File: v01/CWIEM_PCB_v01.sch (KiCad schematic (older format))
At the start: 10 parts

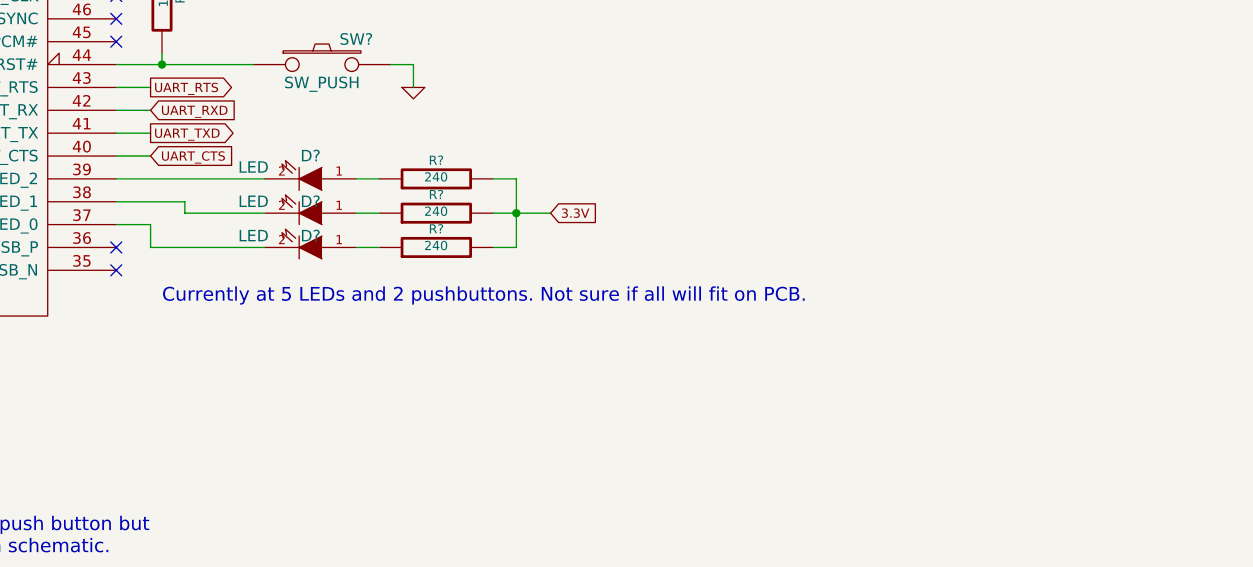
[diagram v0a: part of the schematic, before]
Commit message: Basically just added a single DIP switch to battery charging circuit.
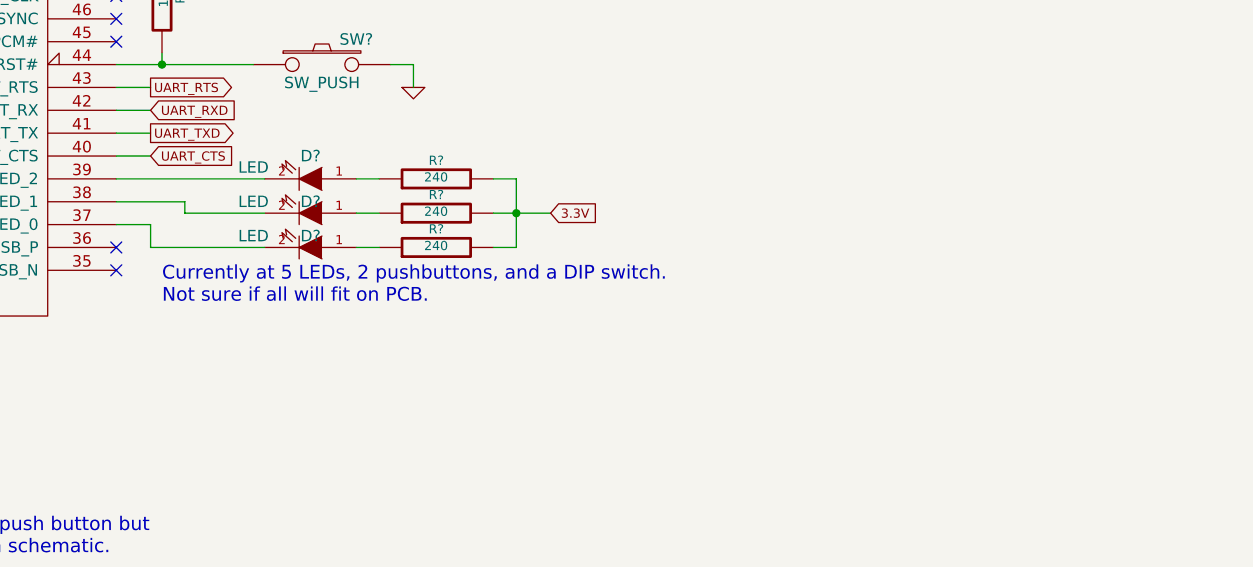
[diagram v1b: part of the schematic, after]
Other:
- note added: "Currently at 5 LEDs, 2 pushbuttons, and a DIP switch. \nNot sure if all will fit on PCB."
- note removed: "Currently at 5 LEDs and 2 pushbuttons. Not sure if all will fit on PCB."
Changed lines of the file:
@@
 Sheet 1 4
 Title "BC127 circuit"
-Date "12 oct 2014"
+Date "18 oct 2014"
 Rev "0"
 Comp ""
@@
 	8050 4300 7950 4300
 Text Notes 7100 4550 0    60   ~ 0
-Currently at 5 LEDs and 2 pushbuttons. Not sure if all will fit on PCB.
+Currently at 5 LEDs, 2 pushbuttons, and a DIP switch. \nNot sure if all will fit on PCB.
 Text Notes 5750 5650 0    60   ~ 0
 There is a mini push button but \nit looks weird in schematic.

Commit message: ERC.
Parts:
- gave numbers to parts that had none: 10
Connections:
- net UART_TXD: no longer U1.29 (CHG_EXT)
- net 3V3_USB: no longer names the net of U1.34 (3V3_USB)
- new net CHG_EXT: U1.29 (CHG_EXT)
- no-connect marks 24 -> 25
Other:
- note added: "I had to make CHG_EXT an output pin \n(base of PNP transistor is an input pin)."
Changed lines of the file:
@@
 Sheet 1 4
 Title "BC127 circuit"
-Date "18 oct 2014"
+Date "25 oct 2014"
 Rev "0"
 Comp ""
@@
 $EndDescr
 $Comp
-L BC127 U?
+L BC127 U1
 U 1 1 541DFC48
 P 5500 3400
-F 0 "U?" H 5500 3300 50  0000 C CNN
+F 0 "U1" H 5500 3300 50  0000 C CNN
 F 1 "BC127" H 5500 3500 50  0000 C CNN
 F 2 "MODULE" H 5500 3400 50  0001 C CNN
@@
 NoConn ~ 6900 4300
 NoConn ~ 6900 4400
-$Comp
-L GND #PWR?
-U 1 1 5439D82F
-P 3350 2700
-F 0 "#PWR?" H 3350 2700 30  0001 C CNN
-F 1 "GND" H 3350 2630 30  0001 C CNN
-F 2 "" H 3350 2700 60  0000 C CNN
-F 3 "" H 3350 2700 60  0000 C CNN
-	1    3350 2700
-	1    0    0    -1
-$EndComp
 NoConn ~ 4100 3300
 NoConn ~ 4100 3200
@@
 NoConn ~ 4100 4400
 $Comp
-L GND #PWR?
+L GND #PWR01
 U 1 1 5439D88D
 P 4900 5000
-F 0 "#PWR?" H 4900 5000 30  0001 C CNN
+F 0 "#PWR01" H 4900 5000 30  0001 C CNN
 F 1 "GND" H 4900 4930 30  0001 C CNN
 F 2 "" H 4900 5000 60  0000 C CNN
@@
 $EndComp
 $Comp
-L GND #PWR?
+L GND #PWR02
 U 1 1 5439D893
 P 5400 5000
-F 0 "#PWR?" H 5400 5000 30  0001 C CNN
+F 0 "#PWR02" H 5400 5000 30  0001 C CNN
 F 1 "GND" H 5400 4930 30  0001 C CNN
 F 2 "" H 5400 5000 60  0000 C CNN
@@
 VBAT_SENSE
 Text GLabel 5600 5000 3    40   Output ~ 0
-UART_TXD
+CHG_EXT
 Text GLabel 5900 5000 3    40   Input ~ 0
 VBAT
 Text GLabel 6000 5000 3    40   Input ~ 0
 3.3V
-Text GLabel 6100 5000 3    40   Input ~ 0
-3V3_USB
 NoConn ~ 6900 3000
 NoConn ~ 6900 3100
@@
 NoConn ~ 6900 3400
 $Comp
-L R R?
+L R R1
 U 1 1 5439DCCE
 P 7100 3200
-F 0 "R?" V 7180 3200 40  0000 C CNN
+F 0 "R1" V 7180 3200 40  0000 C CNN
 F 1 "10k" V 7107 3201 40  0000 C CNN
 F 2 "~" V 7030 3200 30  0000 C CNN
@@
 	7050 3900 6900 3900
 Wire Wire Line
-	4100 2400 3700 2400
-Wire Wire Line
-	3700 2400 3700 3400
-Wire Wire Line
-	3350 2600 4100 2600
-Wire Wire Line
-	4100 2500 3700 2500
-Connection ~ 3700 2500
-Connection ~ 3700 2600
-Wire Wire Line
-	3700 2700 4100 2700
-Wire Wire Line
-	3700 3400 4100 3400
-Connection ~ 3700 2700
-Wire Wire Line
 	5400 4900 5400 5000
 Wire Wire Line
@@
 Wire Wire Line
 	6000 4900 6000 5000
-Wire Wire Line
-	6100 4900 6100 5000
 Wire Wire Line
 	7100 3450 7100 3500
@@
 3.3V
 $Comp
-L R R?
+L R R2
 U 1 1 5439FB11
 P 8300 4000
-F 0 "R?" V 8380 4000 40  0000 C CNN
+F 0 "R2" V 8380 4000 40  0000 C CNN
 F 1 "240" V 8307 4001 40  0000 C CNN
 F 2 "~" V 8230 4000 30  0000 C CNN
@@
 $EndComp
 $Comp
-L R R?
+L R R3
 U 1 1 5439FB19
 P 8300 4150
-F 0 "R?" V 8380 4150 40  0000 C CNN
+F 0 "R3" V 8380 4150 40  0000 C CNN
 F 1 "240" V 8307 4151 40  0000 C CNN
 F 2 "~" V 8230 4150 30  0000 C CNN
@@
 $EndComp
 $Comp
-L R R?
+L R R4
 U 1 1 5439FB1F
 P 8300 4300
-F 0 "R?" V 8380 4300 40  0000 C CNN
+F 0 "R4" V 8380 4300 40  0000 C CNN
 F 1 "240" V 8307 4301 40  0000 C CNN
 F 2 "~" V 8230 4300 30  0000 C CNN
@@
 	6900 3500 7500 3500
 $Comp
-L SW_PUSH SW?
+L SW_PUSH SW2
 U 1 1 5439FEDB
 P 7800 3500
-F 0 "SW?" H 7950 3610 50  0000 C CNN
+F 0 "SW2" H 7950 3610 50  0000 C CNN
 F 1 "SW_PUSH" H 7800 3420 50  0000 C CNN
 F 2 "~" H 7800 3500 60  0000 C CNN
@@
 $EndComp
 $Comp
-L GND #PWR?
+L GND #PWR03
 U 1 1 5439FF2A
 P 8200 3600
-F 0 "#PWR?" H 8200 3600 30  0001 C CNN
+F 0 "#PWR03" H 8200 3600 30  0001 C CNN
 F 1 "GND" H 8200 3530 30  0001 C CNN
 F 2 "" H 8200 3600 60  0000 C CNN
@@
 	8200 3500 8100 3500
 $Comp
-L SW_PUSH SW?
+L SW_PUSH SW1
 U 1 1 5439FFA3
 P 5500 5650
-F 0 "SW?" H 5650 5760 50  0000 C CNN
+F 0 "SW1" H 5650 5760 50  0000 C CNN
 F 1 "SW_PUSH" H 5500 5570 50  0000 C CNN
 F 2 "~" H 5500 5650 60  0000 C CNN
@@
 Wire Wire Line
 	5500 5950 5500 6100
-Wire Wire Line
-	3350 2600 3350 2700
-$Comp
-L LED D?
+$Comp
+L LED D2
 U 1 1 543A005B
 P 7750 4150
-F 0 "D?" H 7750 4100 50  0000 C CNN
+F 0 "D2" H 7750 4100 50  0000 C CNN
 F 1 "LED" H 8000 4100 50  0000 C CNN
 F 2 "~" H 7750 4150 60  0000 C CNN
@@
 $EndComp
 $Comp
-L LED D?
+L LED D1
 U 1 1 543A0079
 P 7750 4000
-F 0 "D?" H 7750 3900 50  0000 C CNN
+F 0 "D1" H 7750 3900 50  0000 C CNN
 F 1 "LED" H 8000 3950 50  0000 C CNN
 F 2 "~" H 7750 4000 60  0000 C CNN
@@
 $EndComp
 $Comp
-L LED D?
+L LED D3
 U 1 1 543A007F
 P 7750 4300
-F 0 "D?" H 7750 4250 50  0000 C CNN
+F 0 "D3" H 7750 4250 50  0000 C CNN
 F 1 "LED" H 8000 4250 50  0000 C CNN
 F 2 "~" H 7750 4300 60  0000 C CNN
@@
 Text Notes 5750 5650 0    60   ~ 0
 There is a mini push button but \nit looks weird in schematic.
+$Comp
+L GND #PWR04
+U 1 1 544AFEB2
+P 3700 2600
+F 0 "#PWR04" H 3700 2600 30  0001 C CNN
+F 1 "GND" H 3700 2530 30  0001 C CNN
+F 2 "" H 3700 2600 60  0000 C CNN
+F 3 "" H 3700 2600 60  0000 C CNN
+	1    3700 2600
+	0    1    1    0
+$EndComp
+Wire Wire Line
+	4100 2600 3700 2600
+Text Notes 6450 5100 0    60   ~ 0
+I had to make CHG_EXT an output pin \n(base of PNP transistor is an input pin).
+NoConn ~ 6100 4900
+Wire Wire Line
+	4100 2500 3850 2500
+Wire Wire Line
+	3850 2400 3850 3400
+Connection ~ 3850 2600
+Wire Wire Line
+	4100 2400 3850 2400
+Connection ~ 3850 2500
+Wire Wire Line
+	3850 2700 4100 2700
+Wire Wire Line
+	3850 3400 4100 3400
+Connection ~ 3850 2700
 $EndSCHEMATC
